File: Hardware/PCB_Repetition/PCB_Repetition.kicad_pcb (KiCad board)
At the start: 4 copper layers, 389.9 x 88.9 mm, 98 parts, among them J1 Conn_01x03, J10 XLR3, J11 XLR3, J12 XLR3, J13 XLR3, J14 XLR3, J15 XLR3, J16 XLR3, J17 XLR3, J18 XLR3, J19 Conn_01x04, J2 XLR3, J20 Conn_01x04, J21 Conn_01x04, J3 XLR3, J4 Conn_01x03, J5 Conn_01x03, J6 Conn_01x03, J7 XLR3, J8 XLR3, J9 XLR3, Q1 SQ2310ES-T1_BE3, Q2 SQ2310ES-T1_BE3, Q3 SQ2310ES-T1_BE3, Q4 SQ2310ES-T1_BE3, Q5 SQ2310ES-T1_BE3, Q6 SQ2310ES-T1_BE3, SW1 SW_SPST, SW2 SW_SPST, SW3 SW_DIP_x02, SW4 SW_DIP_x02, SW5 SW_DIP_x02, SW6 SW_DIP_x02, SW7 SW_DIP_x02, SW8 SW_DIP_x02, SW9 SW_DIP_x02, U2 ZXBM5210-SP, U4 PCF8575DBR

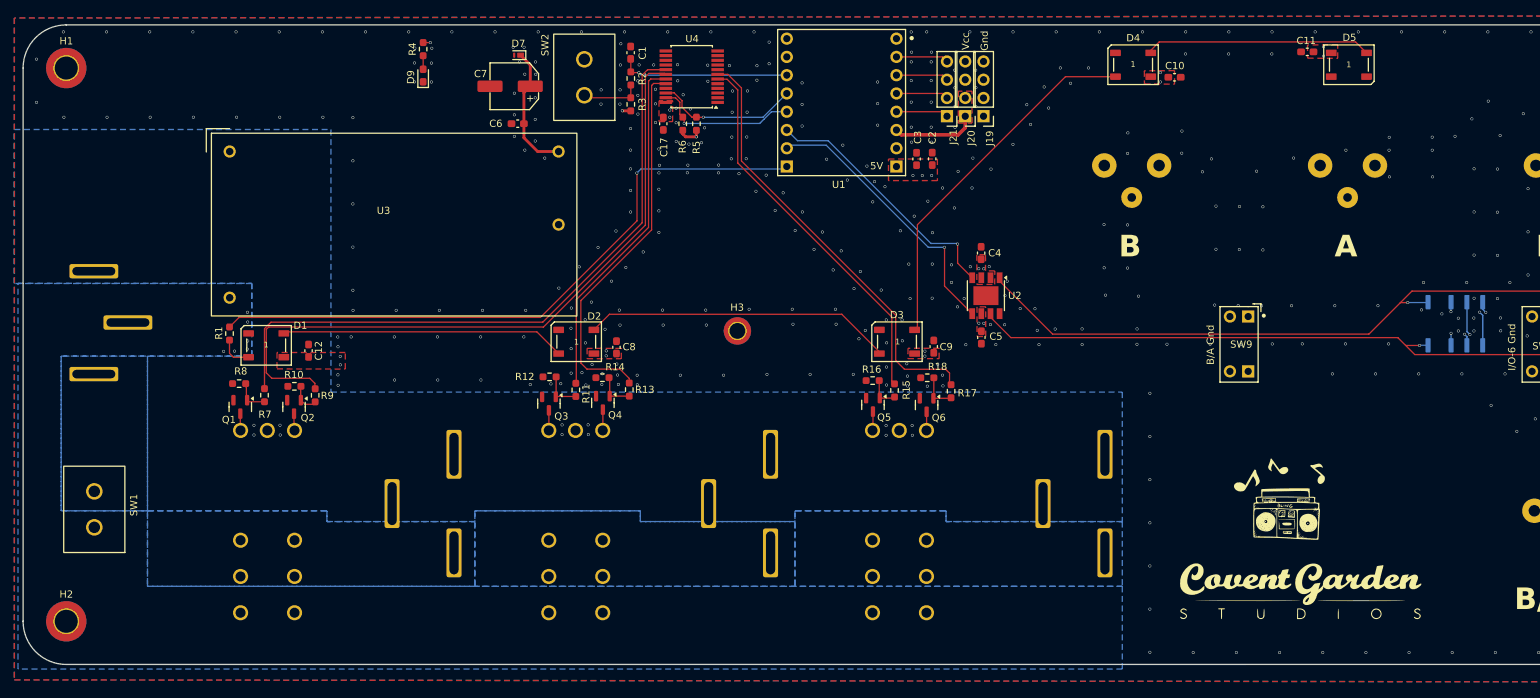
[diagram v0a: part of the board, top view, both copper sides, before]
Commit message: correction orientation des connecteurs sur secteur
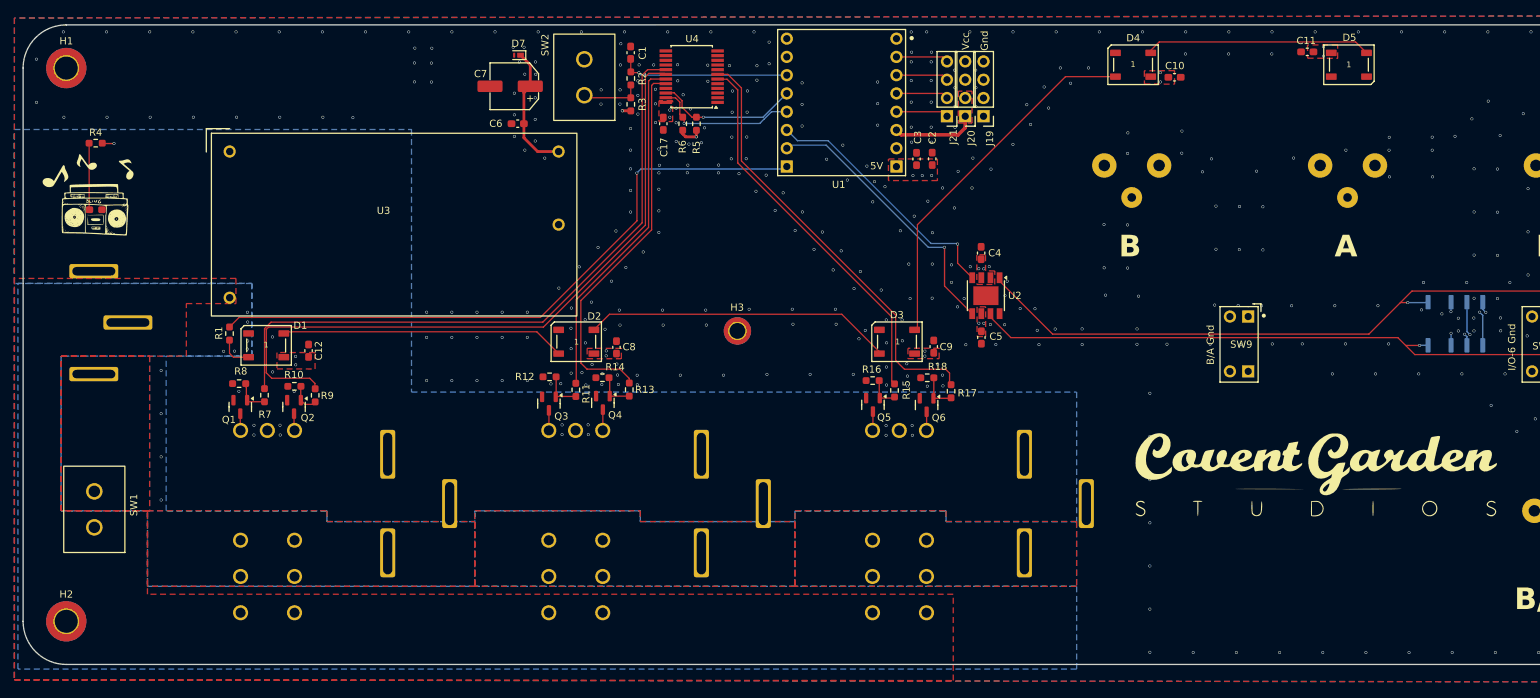
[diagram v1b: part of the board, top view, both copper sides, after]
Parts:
- removed the G*** at (208.8, 214.7)
- removed the G*** at (211.4, 227.6)
- removed the G*** at (83.5, 176.9)
- added G***: LOGO, img:grand_logo_covent, F.Cu at (213.6, 211.5)
- added G***: LOGO, img:grand_logo_covent, B.Cu at (136.2, 181.1)
- added G***: LOGO, img:dessin_musique, B.Cu at (216.2, 221.4)
- D9: footprint LED_SMD:LED_0603_1608Metric_Pad1.05x0.95mm_HandSolder -> img:LED_0603_avec_dessin
- moved G*** 136.2 mm to (206.2, 224.9)
- moved D9 49.3 mm to (43.8, 174.6), turned to 0 degrees
- moved R4 47.4 mm to (43.8, 164.9), turned to 180 degrees
- moved J4 8.00 mm to (93.0, 215.0), turned to -90 degrees
- moved J5 7.60 mm to (136.6, 215.0), turned to -90 degrees
- moved J6 6.02 mm to (181.5, 215.0), turned to -90 degrees
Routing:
- net Net-(D9-A): track 1.88 -> 9.27 mm
- net +5V: track 23.7 -> 24.3 mm
- net GND: vias 789 -> 790
- added copper zone on F.Cu, net /Phase
- added copper zone on F.Cu, net /Relais1/LINE_Sw
- added copper zone on F.Cu, net /Relais2/LINE_Sw
- added copper zone on F.Cu, net /Relais3/LINE_Sw
- added copper zone on F.Cu, net LINE
